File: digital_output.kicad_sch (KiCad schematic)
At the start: 1 part

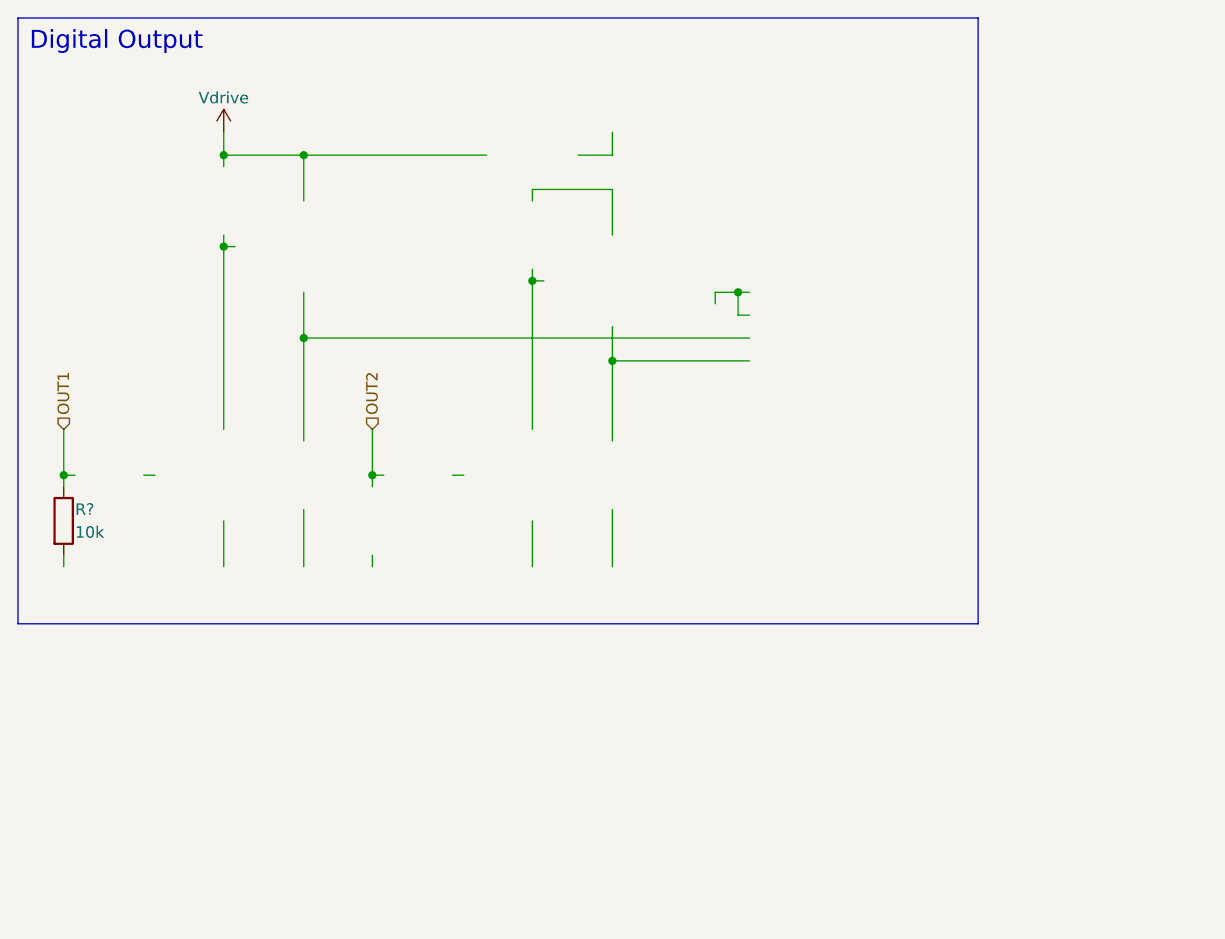
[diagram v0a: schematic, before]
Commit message: recovery of schematics while keeping routed traces
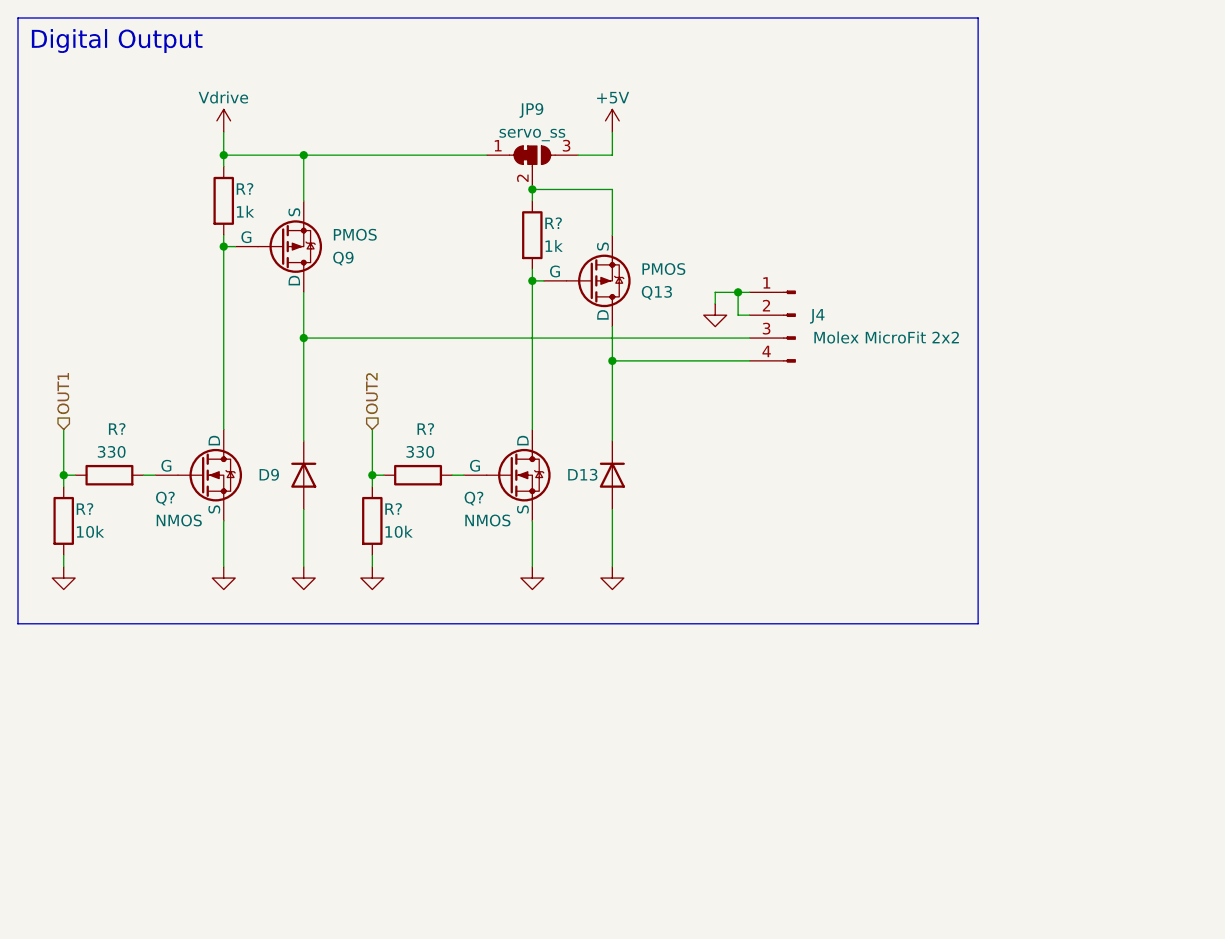
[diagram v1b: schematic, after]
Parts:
- added D13, D9: D, Diode_SMD:D_SOD-123F, symbol Device:D
- added J4: Molex MicroFit 2x2, Connector_Molex:Molex_Micro-Fit_3.0_43045-0400_2x02_P3.00mm_Horizontal, symbol Connector:Conn_01x04_Pin
- added JP9: servo_ss, Jumper:SolderJumper-3_P1.3mm_Open_RoundedPad1.0x1.5mm, symbol Jumper:SolderJumper_3_Bridged12
- added Q13, Q9: PMOS, Package_TO_SOT_SMD:SOT-23, symbol Simulation_SPICE:PMOS
- added Q? (x2): NMOS, Package_TO_SOT_SMD:SOT-23, symbol Simulation_SPICE:NMOS
- added R? (x2): 1k, Resistor_SMD:R_0603_1608Metric_Pad0.98x0.95mm_HandSolder, symbol Device:R
- added R? (x2): 330, Resistor_SMD:R_0603_1608Metric_Pad0.98x0.95mm_HandSolder, symbol Device:R
- added R?: 10k, Resistor_SMD:R_0603_1608Metric_Pad0.98x0.95mm_HandSolder, symbol Device:R
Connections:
- net OUT1: now also R?.1
- net OUT2: now also R?.1, R?.1
- net Vdrive: now also JP9.1 (A), Q9.3 (S), R?.1
- net GND: now reaches R?.2
- net GND: now also D13.2 (A), D9.2 (A), J4.1 (Pin_1), J4.2 (Pin_2), Q?.3 (S), Q?.3 (S), R?.2
- new net: Q13.2 (G), Q?.1 (D), R?.2
- new net: Q?.2 (G), R?.2 (x2)
- new net: JP9.2 (C), Q13.3 (S), R?.1
- new net: Q9.2 (G), Q?.1 (D), R?.2
- new net: D13.1 (K), J4.4 (Pin_4), Q13.1 (D)
- new net: D9.1 (K), J4.3 (Pin_3), Q9.1 (D)
- new net +5V: JP9.3 (B)

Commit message: add descriptors on silkscreen, add part numbers
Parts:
- D13, D9: LCSC# (none) -> C167645; Manufacturer (none) -> Nexperia; Part# (none) -> PMEG3020EH,115
- J4, JP9: LCSC# (none) -> x
- Q13, Q9: LCSC# (none) -> C15127; Manufacturer (none) -> Alpha & Omega Semicon; Part# (none) -> AO3401A
- Q? (x2): LCSC# (none) -> C20917; Manufacturer (none) -> Alpha & Omega Semicon; Part# (none) -> AO3400A
- R? (x2): LCSC# (none) -> C25804; Manufacturer (none) -> UNI-ROYAL(Uniroyal Elec)
- R? (x2): LCSC# (none) -> C21190; Manufacturer (none) -> UNI-ROYAL(Uniroyal Elec)
- R? (x2): LCSC# (none) -> C23138; Manufacturer (none) -> UNI-ROYAL(Uniroyal Elec)
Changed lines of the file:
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@@
+      (effects (font (size 1.27 1.27)) hide)
+    )
+    (property "LCSC#" "C25804" (at 19.05 69.85 0)
+      (effects (font (size 1.27 1.27)) hide)
+    )
+    (property "Manufacturer" "UNI-ROYAL(Uniroyal Elec)" (at 19.05 69.85 0)
       (effects (font (size 1.27 1.27)) hide)
     )
@@
       (effects (font (size 1.27 1.27)) hide)
     )
+    (property "LCSC#" "C20917" (at 68.58 64.77 0)
+      (effects (font (size 1.27 1.27)) hide)
+    )
+    (property "Manufacturer" "Alpha & Omega Semicon" (at 68.58 64.77 0)
+      (effects (font (size 1.27 1.27)) hide)
+    )
+    (property "Part#" "AO3400A" (at 68.58 64.77 0)
+      (effects (font (size 1.27 1.27)) hide)
+    )
     (pin "1")
     (pin "3")
@@
       (effects (font (size 1.27 1.27)) hide)
     )
+    (property "LCSC#" "C21190" (at 71.12 38.1 0)
+      (effects (font (size 1.27 1.27)) hide)
+    )
+    (property "Manufacturer" "UNI-ROYAL(Uniroyal Elec)" (at 71.12 38.1 0)
+      (effects (font (size 1.27 1.27)) hide)
+    )
     (pin "2")
     (pin "1")
@@
     )
     (property "Datasheet" "~" (at 36.83 34.29 0)
+      (effects (font (size 1.27 1.27)) hide)
+    )
+    (property "LCSC#" "C21190" (at 36.83 34.29 0)
+      (effects (font (size 1.27 1.27)) hide)
+    )
+    (property "Manufacturer" "UNI-ROYAL(Uniroyal Elec)" (at 36.83 34.29 0)
       (effects (font (size 1.27 1.27)) hide)
     )
@@
       (effects (font (size 1.27 1.27)) hide)
     )
+    (property "LCSC#" "C23138" (at 24.13 64.77 0)
+      (effects (font (size 1.27 1.27)) hide)
+    )
+    (property "Manufacturer" "UNI-ROYAL(Uniroyal Elec)" (at 24.13 64.77 0)
+      (effects (font (size 1.27 1.27)) hide)
+    )
     (pin "2")
     (pin "1")
@@
       (effects (font (size 1.27 1.27)) hide)
     )
+    (property "LCSC#" "C167645" (at 80.01 64.77 0)
+      (effects (font (size 1.27 1.27)) hide)
+    )
+    (property "Manufacturer" "Nexperia" (at 80.01 64.77 0)
+      (effects (font (size 1.27 1.27)) hide)
+    )
+    (property "Part#" "PMEG3020EH,115" (at 80.01 64.77 0)
+      (effects (font (size 1.27 1.27)) hide)
+    )
     (pin "1")
     (pin "2")
@@
     )
     (property "Sim.Pins" "1=D 2=G 3=S" (at 43.18 24.13 0)
+      (effects (font (size 1.27 1.27)) hide)
+    )
+    (property "LCSC#" "C15127" (at 43.18 39.37 0)
+      (effects (font (size 1.27 1.27)) hide)
+    )
+    (property "Manufacturer" "Alpha & Omega Semicon" (at 43.18 39.37 0)
+      (effects (font (size 1.27 1.27)) hide)
+    )
+    (property "Part#" "AO3401A" (at 43.18 39.37 0)
       (effects (font (size 1.27 1.27)) hide)
     )
@@
       (effects (font (size 1.27 1.27)) hide)
     )
+    (property "LCSC#" "x" (at 71.12 29.21 0)
+      (effects (font (size 1.27 1.27)) hide)
+    )
     (pin "2")
     (pin "3")
@@
       (effects (font (size 1.27 1.27)) hide)
     )
+    (property "LCSC#" "C167645" (at 45.72 64.77 0)
+      (effects (font (size 1.27 1.27)) hide)
+    )
+    (property "Manufacturer" "Nexperia" (at 45.72 64.77 0)
+      (effects (font (size 1.27 1.27)) hide)
+    )
+    (property "Part#" "PMEG3020EH,115" (at 45.72 64.77 0)
+      (effects (font (size 1.27 1.27)) hide)
+    )
     (pin "1")
     (pin "2")
@@
     )
     (property "Datasheet" "~" (at 58.42 64.77 0)
+      (effects (font (size 1.27 1.27)) hide)
+    )
+    (property "LCSC#" "C23138" (at 58.42 64.77 0)
+      (effects (font (size 1.27 1.27)) hide)
+    )
+    (property "Manufacturer" "UNI-ROYAL(Uniroyal Elec)" (at 58.42 64.77 0)
       (effects (font (size 1.27 1.27)) hide)
     )
@@
       (effects (font (size 1.27 1.27)) hide)
     )
+    (property "LCSC#" "C20917" (at 34.29 64.77 0)
+      (effects (font (size 1.27 1.27)) hide)
+    )
+    (property "Manufacturer" "Alpha & Omega Semicon" (at 34.29 64.77 0)
+      (effects (font (size 1.27 1.27)) hide)
+    )
+    (property "Part#" "AO3400A" (at 34.29 64.77 0)
+      (effects (font (size 1.27 1.27)) hide)
+    )
     (pin "3")
     (pin "2")
@@
       (effects (font (size 1.27 1.27)) hide)
     )
+    (property "LCSC#" "C25804" (at 53.34 69.85 0)
+      (effects (font (size 1.27 1.27)) hide)
+    )
+    (property "Manufacturer" "UNI-ROYAL(Uniroyal Elec)" (at 53.34 69.85 0)
+      (effects (font (size 1.27 1.27)) hide)
+    )
     (pin "2")
     (pin "1")
@@
     )
     (property "Sim.Pins" "1=D 2=G 3=S" (at 77.47 27.94 0)
+      (effects (font (size 1.27 1.27)) hide)
+    )
+    (property "LCSC#" "C15127" (at 77.47 43.18 0)
+      (effects (font (size 1.27 1.27)) hide)
+    )
+    (property "Manufacturer" "Alpha & Omega Semicon" (at 77.47 43.18 0)
+      (effects (font (size 1.27 1.27)) hide)
+    )
+    (property "Part#" "AO3401A" (at 77.47 43.18 0)
       (effects (font (size 1.27 1.27)) hide)
     )
@@
       (effects (font (size 1.27 1.27)) hide)
     )
+    (property "LCSC#" "x" (at 100.33 46.99 0)
+      (effects (font (size 1.27 1.27)) hide)
+    )

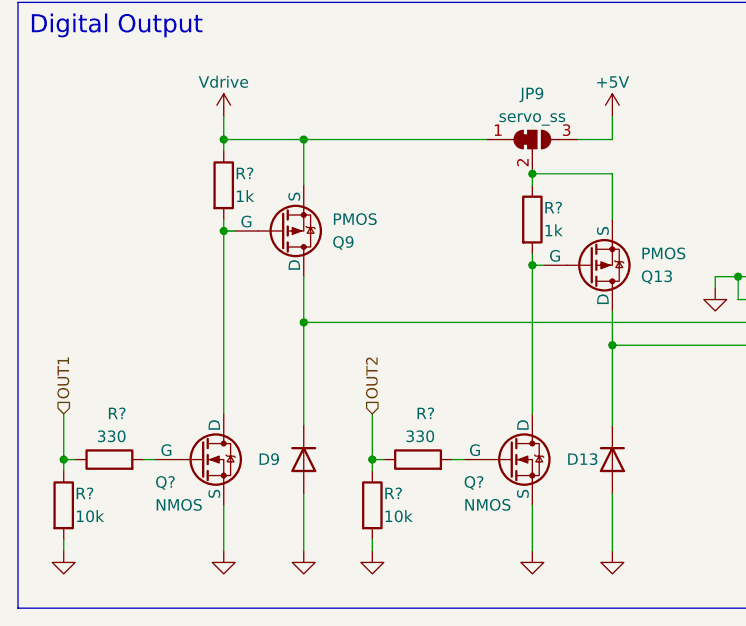
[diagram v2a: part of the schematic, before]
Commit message: removed boost converter
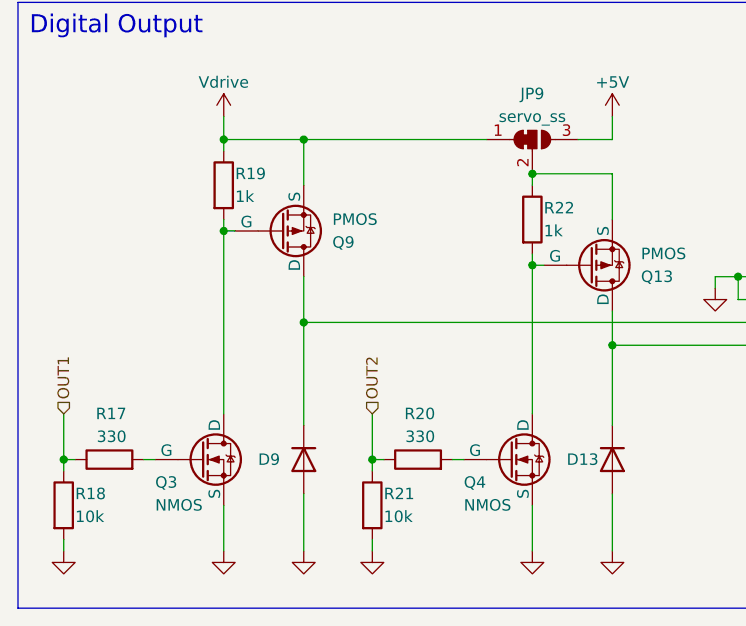
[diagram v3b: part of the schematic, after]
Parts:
- gave numbers to parts that had none: 8

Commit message: minor changes
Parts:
- renumbered J4 to J9

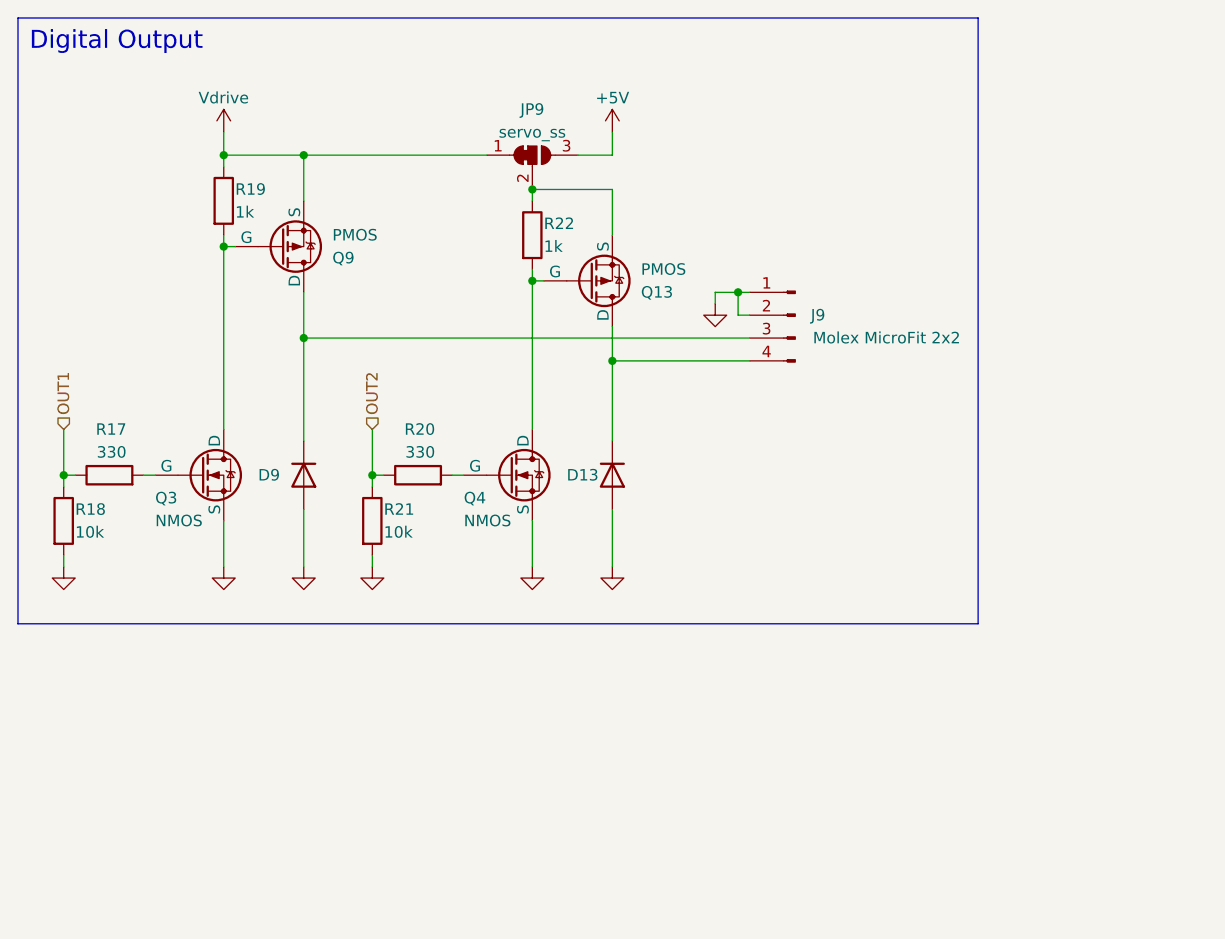
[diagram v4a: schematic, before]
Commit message: updated scematic to new requirements
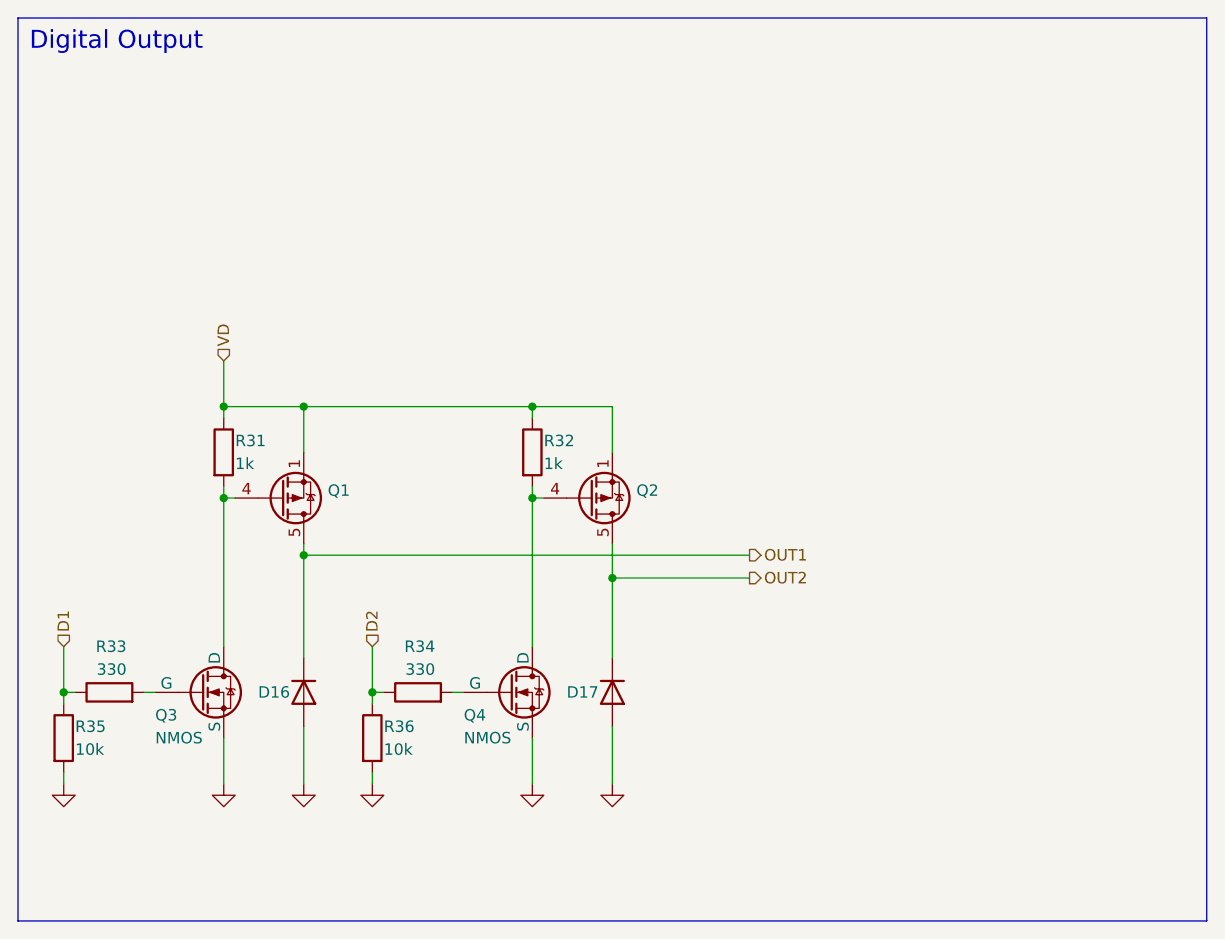
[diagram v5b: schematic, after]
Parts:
- removed J9: Molex MicroFit 2x2, Connector_Molex:Molex_Micro-Fit_3.0_43045-0400_2x02_P3.00mm_Horizontal, symbol Connector:Conn_01x04_Pin
- removed JP9: servo_ss, Jumper:SolderJumper-3_P1.3mm_Open_RoundedPad1.0x1.5mm, symbol Jumper:SolderJumper_3_Bridged12
- removed Q13, Q9: PMOS, Package_TO_SOT_SMD:SOT-23, symbol Simulation_SPICE:PMOS
- added Q1, Q2: AOSP21321, Package_SO:SO-8_3.9x4.9mm_P1.27mm, symbol euroc_fc:AOSP21321
- renumbered D9 to D16, D13 to D17, R19 to R31, R22 to R32, R17 to R33, R20 to R34, R18 to R35, R21 to R36
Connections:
- net Vdrive is gone; now on net VD: R31.1
- net OUT1: now also D16.1 (K), Q1.5 (D), Q1.6 (D), Q1.7 (D), Q1.8 (D); no longer R33.1, R35.1
- net OUT2: now also D17.1 (K), Q2.5 (D), Q2.6 (D), Q2.7 (D), Q2.8 (D); no longer R34.1, R36.1
- net at Q4.1 (D), R32.2: now also Q2.4 (G)
- net VD: now reaches R32.1
- net VD: now also Q1.1 (S), Q1.2 (S), Q1.3 (S), Q2.1 (S), Q2.2 (S), Q2.3 (S)
- net at Q3.1 (D), R31.2: now also Q1.4 (G)
- new net D1: R33.1, R35.1
- new net D2: R34.1, R36.1
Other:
- moved on the sheet: D16, D17, Q3, Q4, R31, R32, R33, R34, R35, R36

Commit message: some more changes to the io board
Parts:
- removed D16, D17: D, Diode_SMD:D_SOD-123F, symbol Device:D
- added D21, D23: D, Diode_SMD:D_SOD-323_HandSoldering, symbol Device:D
- renumbered R31 to R40, R32 to R41, R33 to R42, R34 to R43, R35 to R44, R36 to R45
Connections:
- net GND: now also D21.2 (A), D23.2 (A)
- net OUT1: now also D23.1 (K)
- net OUT2: now also D21.1 (K)
